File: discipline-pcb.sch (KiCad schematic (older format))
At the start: 22 parts, among them J1 AVR-ISP-6, U1 ATmega32A-PU, Y1 Crystal

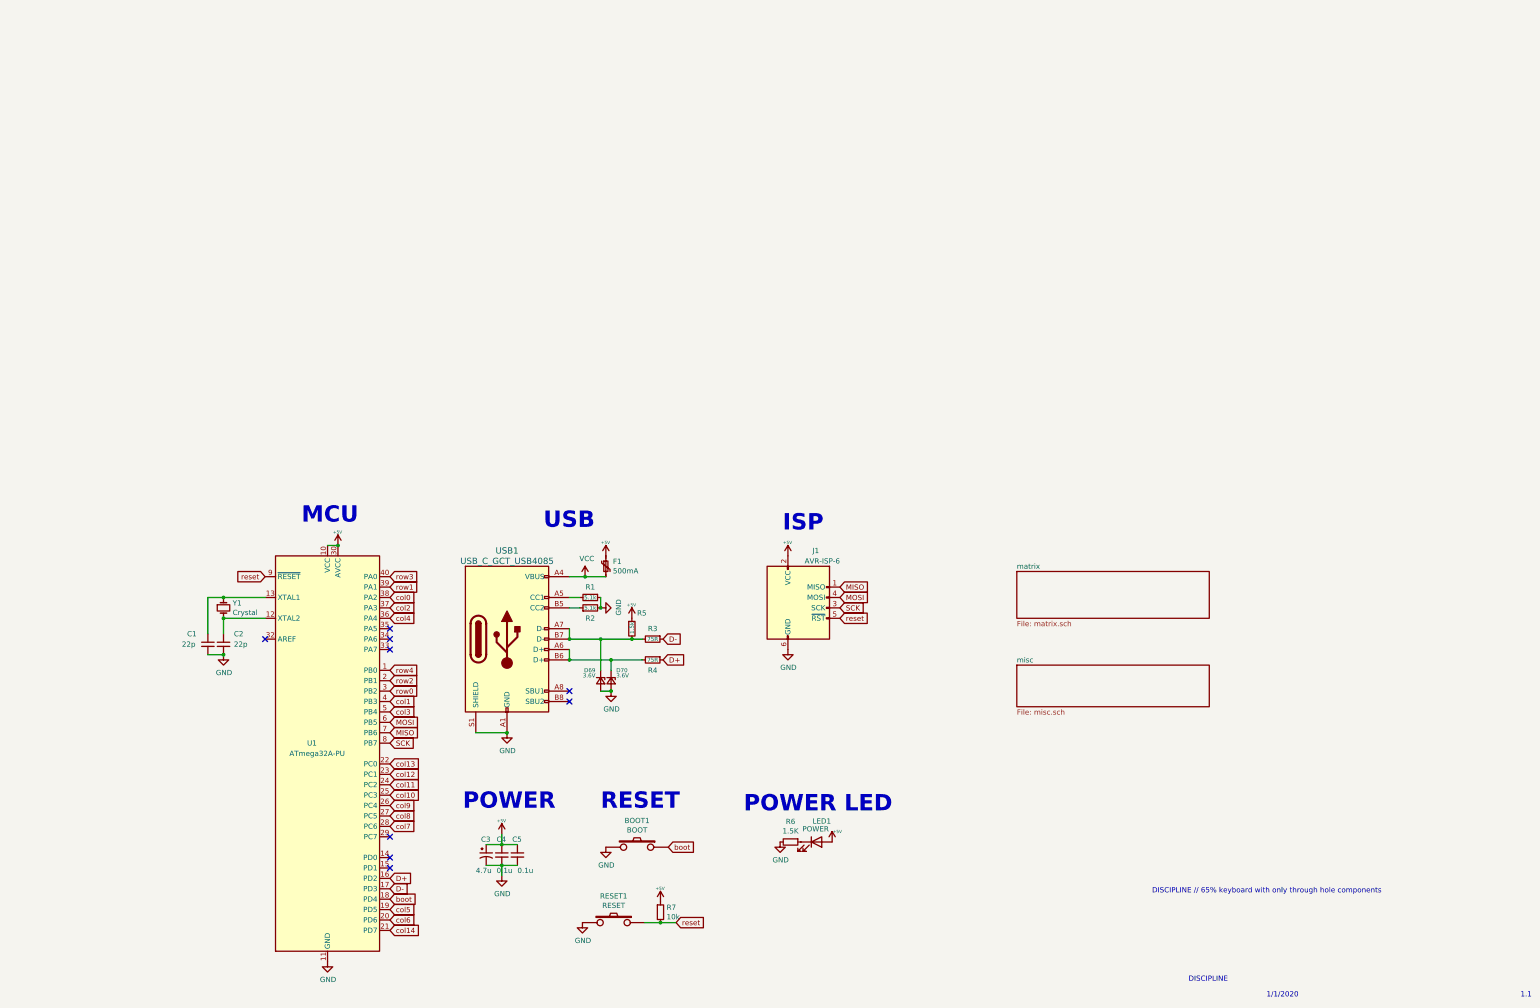
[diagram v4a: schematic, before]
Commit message: Add power, oled, ble modules
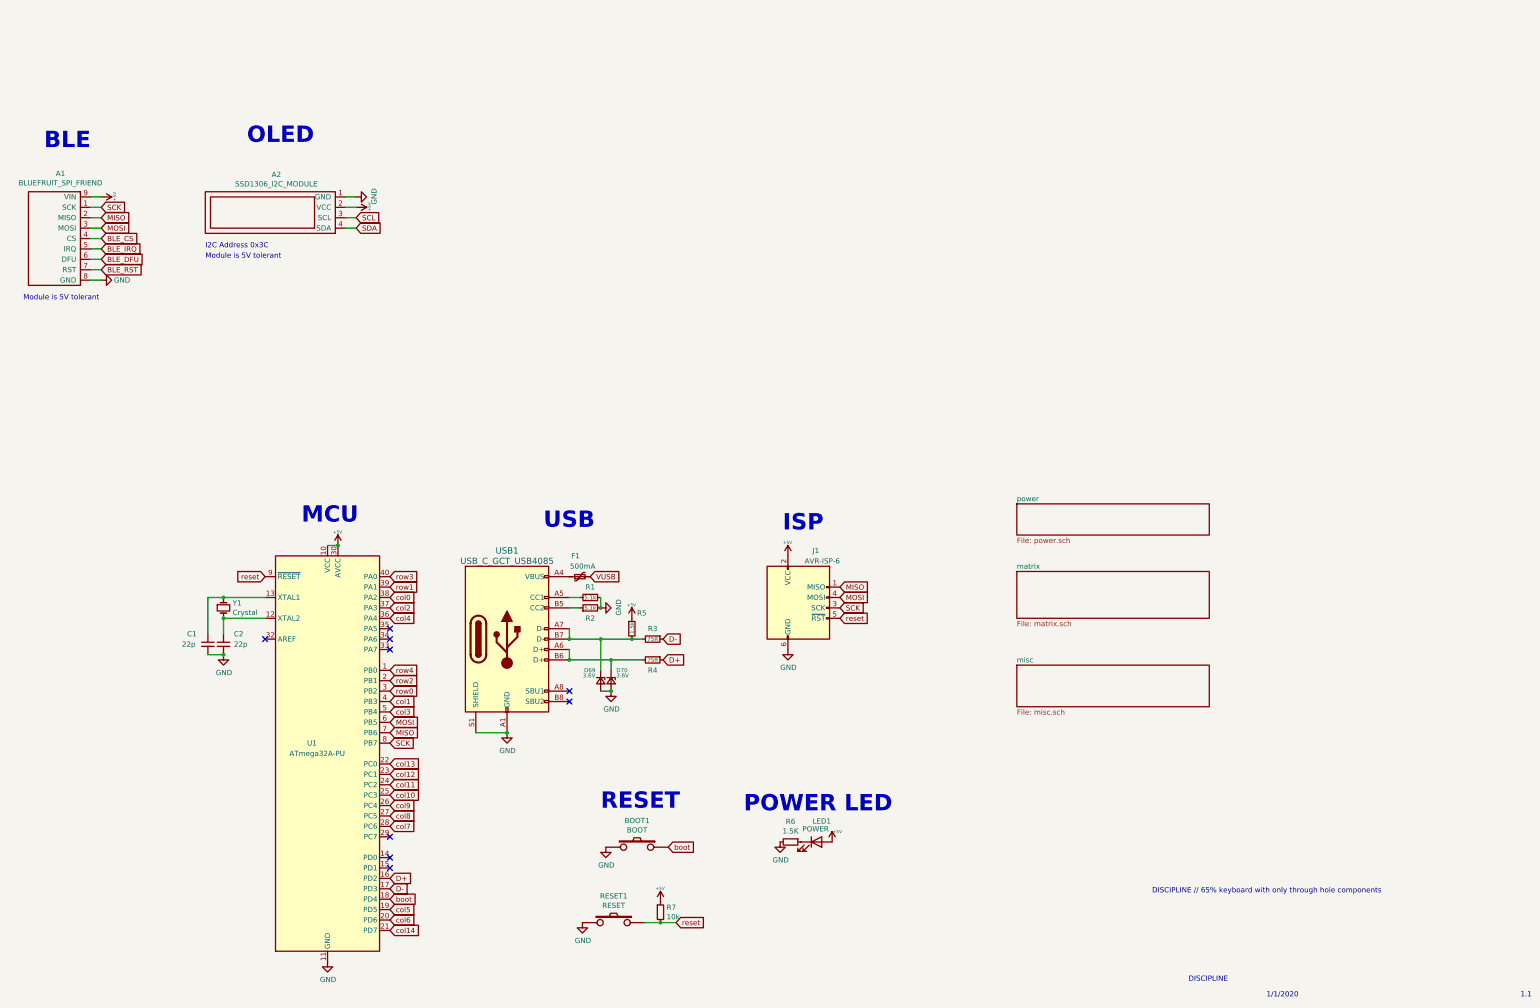
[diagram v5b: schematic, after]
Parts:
- removed C3: 4.7u, cftkb:CP_Radial_D4.0mm_P1.50mm, symbol Device:CP1_Small
- removed C4, C5: 0.1u, cftkb:C_Disc_D4.3mm_W1.9mm_P5.00mm, symbol Device:C_Small
- added A1: BLUEFRUIT_SPI_FRIEND, Gigahawk:BLUEFRUIT_SPI_FRIEND, symbol gigahawk:BLUEFRUIT_SPI_FRIEND
- added A2: SSD1306_I2C_MODULE, Gigahawk:SSD1306_MODULE_128x32, symbol gigahawk:SSD1306_I2C_MODULE
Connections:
- net +5V: now also A1.9 (VIN), A2.2 (VCC); no longer F1.1
- net GND: now also A1.8 (GND), A2.1 (GND)
- net MISO: now also A1.2 (MISO)
- net MOSI: now also A1.3 (MOSI)
- net SCK: now also A1.1 (SCK)
- net VCC: no longer names the net of USB1.A4 (VBUS), USB1.A9 (VBUS), USB1.B4 (VBUS), USB1.B9 (VBUS)
- net VCC: now also F1.1; no longer F1.2
- new net BLE_CS: A1.4 (CS)
- new net BLE_DFU: A1.6 (DFU)
- new net BLE_IRQ: A1.5 (IRQ)
- new net BLE_RST: A1.7 (RST)
- new net SCL: A2.3 (SCL)
- new net SDA: A2.4 (SDA)
- new net VUSB: F1.2
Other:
- note added: "BLE"
- note added: "I2C Address 0x3C"
- note added: "Module is 5V tolerant"
- note added: "Module is 5V tolerant\n"
- note added: "OLED"
- note removed: "POWER"
- moved on the sheet: F1
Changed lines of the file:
@@
 $Descr A3 16535 11693
 encoding utf-8
-Sheet 1 3
+Sheet 1 4
 Title ""
 Date ""
@@
 $EndComp
 $Comp
-L power:VCC #PWR0105
-U 1 1 5D2F7246
-P 6450 7000
-F 0 "#PWR0105" H 6450 6850 50  0001 C CNN
-F 1 "VCC" H 6467 7173 50  0000 C CNN
-F 2 "" H 6450 7000 50  0001 C CNN
-F 3 "" H 6450 7000 50  0001 C CNN
-	1    6450 7000
-	1    0    0    -1
-$EndComp
-$Comp
 L Device:Polyfuse_Small F1
 U 1 1 5D2F73B7
-P 6650 6900
-F 0 "F1" H 6718 6946 50  0000 L CNN
-F 1 "500mA" H 6718 6855 50  0000 L CNN
-F 2 "cftkb:polyfuse_5.1mm" H 6700 6700 50  0001 L CNN
-F 3 "~" H 6650 6900 50  0001 C CNN
-	1    6650 6900
-	1    0    0    -1
+P 6400 7000
+F 0 "F1" V 6600 7000 50  0000 L CNN
+F 1 "500mA" V 6500 6850 50  0000 L CNN
+F 2 "cftkb:polyfuse_5.1mm" H 6450 6800 50  0001 L CNN
+F 3 "~" H 6400 7000 50  0001 C CNN
+	1    6400 7000
+	0    -1   -1   0
 $EndComp
 $Comp
 L power:+5V #PWR0110
 U 1 1 5D31262D
-P 6650 6800
-F 0 "#PWR0110" H 6650 6890 20  0001 C CNN
-F 1 "+5V" H 6646 6928 30  0000 C CNN
-F 2 "" H 6650 6800 60  0000 C CNN
-F 3 "" H 6650 6800 60  0000 C CNN
-	1    6650 6800
-	1    0    0    -1
-$EndComp
-$Comp
-L Device:CP1_Small C3
-U 1 1 5D175B8C
-P 5500 9675
-F 0 "C3" H 5450 9825 50  0000 L CNN
-F 1 "4.7u" H 5400 9525 50  0000 L CNN
-F 2 "cftkb:CP_Radial_D4.0mm_P1.50mm" H 5500 9675 50  0001 C CNN
-F 3 "~" H 5500 9675 50  0001 C CNN
-	1    5500 9675
-	1    0    0    -1
-$EndComp
-$Comp
-L Device:C_Small C4
-U 1 1 5D176D89
-P 5650 9675
-F 0 "C4" H 5600 9825 50  0000 L CNN
-F 1 "0.1u" H 5600 9525 50  0000 L CNN
-F 2 "cftkb:C_Disc_D4.3mm_W1.9mm_P5.00mm" H 5650 9675 50  0001 C CNN
-F 3 "~" H 5650 9675 50  0001 C CNN
-	1    5650 9675
-	1    0    0    -1
-$EndComp
-$Comp
-L Device:C_Small C5
-U 1 1 5D176ED3
-P 5800 9675
-F 0 "C5" H 5750 9825 50  0000 L CNN
-F 1 "0.1u" H 5800 9525 50  0000 L CNN
-F 2 "cftkb:C_Disc_D4.3mm_W1.9mm_P5.00mm" H 5800 9675 50  0001 C CNN
-F 3 "~" H 5800 9675 50  0001 C CNN
-	1    5800 9675
-	1    0    0    -1
-$EndComp
-Wire Wire Line
-	5500 9575 5650 9575
-Connection ~ 5650 9575
-Wire Wire Line
-	5650 9575 5800 9575
-$Comp
-L power:+5V #PWR0111
-U 1 1 5D193DAD
-P 5650 9475
-F 0 "#PWR0111" H 5650 9565 20  0001 C CNN
-F 1 "+5V" H 5646 9603 30  0000 C CNN
-F 2 "" H 5650 9475 60  0000 C CNN
-F 3 "" H 5650 9475 60  0000 C CNN
-	1    5650 9475
-	1    0    0    -1
-$EndComp
-Wire Wire Line
-	5650 9575 5650 9475
-Wire Wire Line
-	5500 9775 5650 9775
-Connection ~ 5650 9775
-Wire Wire Line
-	5650 9775 5800 9775
-Wire Wire Line
-	5650 9775 5650 9875
+P 1800 3350
+F 0 "#PWR0110" H 1800 3440 20  0001 C CNN
+F 1 "+5V" H 1796 3478 30  0000 C CNN
+F 2 "" H 1800 3350 60  0000 C CNN
+F 3 "" H 1800 3350 60  0000 C CNN
+	1    1800 3350
+	0    1    1    0
+$EndComp
 $Comp
 L power:+5V #PWR0108
@@
 NoConn ~ 4575 9800
 $Comp
-L power:GND #PWR0112
-U 1 1 5DA49277
-P 5650 9875
-F 0 "#PWR0112" H 5650 9625 50  0001 C CNN
-F 1 "GND" H 5655 9702 50  0000 C CNN
-F 2 "" H 5650 9875 50  0001 C CNN
-F 3 "" H 5650 9875 50  0001 C CNN
-	1    5650 9875
-	1    0    0    -1
-$EndComp
-$Comp
 L MCU_Microchip_ATmega:ATmega32A-PU U1
 U 1 1 5DF0B623
@@
 Text Notes 8350 6575 0    157  ~ 31
 ISP
-Text Notes 5275 9250 0    157  ~ 31
-POWER
 Text Notes 6600 9250 0    157  ~ 31
 RESET
@@
 	1    0    0    -1
 $EndComp
-Wire Wire Line
-	6300 7000 6450 7000
-Wire Wire Line
-	6450 7000 6650 7000
-Connection ~ 6450 7000
 Wire Wire Line
 	5400 8500 5700 8500
@@
 F1 "misc.sch" 50
 $EndSheet
+$Comp
+L gigahawk:SSD1306_I2C_MODULE A2
+U 1 1 5F28E9FA
+P 4050 3300
+F 0 "A2" H 4617 3135 50  0000 C CNN
+F 1 "SSD1306_I2C_MODULE" H 4617 3226 50  0000 C CNN
+F 2 "Gigahawk:SSD1306_MODULE_128x32" H 4650 3750 50  0001 C CNN
+F 3 "" H 4100 3450 50  0001 C CNN
+	1    4050 3300
+	-1   0    0    1
+$EndComp
+$Comp
+L gigahawk:BLUEFRUIT_SPI_FRIEND A1
+U 1 1 5F29009B
+P 1350 3750
+F 0 "A1" H 1408 4375 50  0000 C CNN
+F 1 "BLUEFRUIT_SPI_FRIEND" H 1408 4284 50  0000 C CNN
+F 2 "Gigahawk:BLUEFRUIT_SPI_FRIEND" H 700 4150 50  0001 C CNN
+F 3 "" H 700 4150 50  0001 C CNN
+	1    1350 3750
+	1    0    0    -1
+$EndComp
+Text GLabel 6500 7000 2    50   Input ~ 0
+VUSB
+$Sheet
+S 10600 6300 1850 300
+U 5F36D657
+F0 "power" 50
+F1 "power.sch" 50
+$EndSheet
+Text Notes 1250 2900 0    157  ~ 31
+BLE
+Wire Wire Line
+	1700 3350 1800 3350
+Text GLabel 1800 3650 2    50   Input ~ 0
+MOSI
+Text GLabel 1800 3550 2    50   Input ~ 0
+MISO
+Text GLabel 1800 3450 2    50   Input ~ 0
+SCK
+Text GLabel 1800 3750 2    50   Input ~ 0
+BLE_CS
+Text GLabel 1800 3850 2    50   Input ~ 0
+BLE_IRQ
+Text GLabel 1800 3950 2    50   Input ~ 0
+BLE_DFU
+Text GLabel 1800 4050 2    50   Input ~ 0
+BLE_RST
+$Comp
+L power:GND #PWR?
+U 1 1 5F37DA59
+P 1800 4150
+F 0 "#PWR?" H 1800 3900 50  0001 C CNN
+F 1 "GND" V 1800 3950 50  0000 C CNN
+F 2 "" H 1800 4150 50  0001 C CNN
+F 3 "" H 1800 4150 50  0001 C CNN
+	1    1800 4150
+	0    -1   -1   0
+$EndComp
+Wire Wire Line
+	1700 4150 1800 4150
+Wire Wire Line
+	1700 4050 1800 4050
+Wire Wire Line
+	1700 3950 1800 3950
+Wire Wire Line
+	1700 3850 1800 3850
+Wire Wire Line
+	1700 3750 1800 3750
+Wire Wire Line
+	1700 3650 1800 3650
+Wire Wire Line
+	1700 3550 1800 3550
+Wire Wire Line
+	1700 3450 1800 3450
+Text Notes 3200 2850 0    157  ~ 31
+OLED
+$Comp
+L power:GND #PWR?
+U 1 1 5F38423A
+P 4250 3350
+F 0 "#PWR?" H 4250 3100 50  0001 C CNN
+F 1 "GND" H 4255 3177 50  0000 C CNN
+F 2 "" H 4250 3350 50  0001 C CNN
+F 3 "" H 4250 3350 50  0001 C CNN
+	1    4250 3350
+	0    -1   -1   0
+$EndComp
+Text Notes 1050 4350 0    50   ~ 0
+Module is 5V tolerant\n
+Text Notes 2800 3950 0    50   ~ 0
+Module is 5V tolerant
+Wire Wire Line
+	4150 3350 4250 3350
+$Comp
+L power:+5V #PWR?
+U 1 1 5F385D89
+P 4250 3450
+F 0 "#PWR?" H 4250 3540 20  0001 C CNN
+F 1 "+5V" H 4246 3578 30  0000 C CNN
+F 2 "" H 4250 3450 60  0000 C CNN
+F 3 "" H 4250 3450 60  0000 C CNN
+	1    4250 3450
+	0    1    1    0
+$EndComp
+Wire Wire Line
+	4150 3450 4250 3450
+Text GLabel 4250 3550 2    50   Input ~ 0
+SCL
+Text GLabel 4250 3650 2    50   Input ~ 0
+SDA
+Wire Wire Line
+	4150 3550 4250 3550
+Wire Wire Line
+	4150 3650 4250 3650
+Text Notes 2800 3850 0    50   ~ 0
+I2C Address 0x3C
 $EndSCHEMATC

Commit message: Add rotary encoder
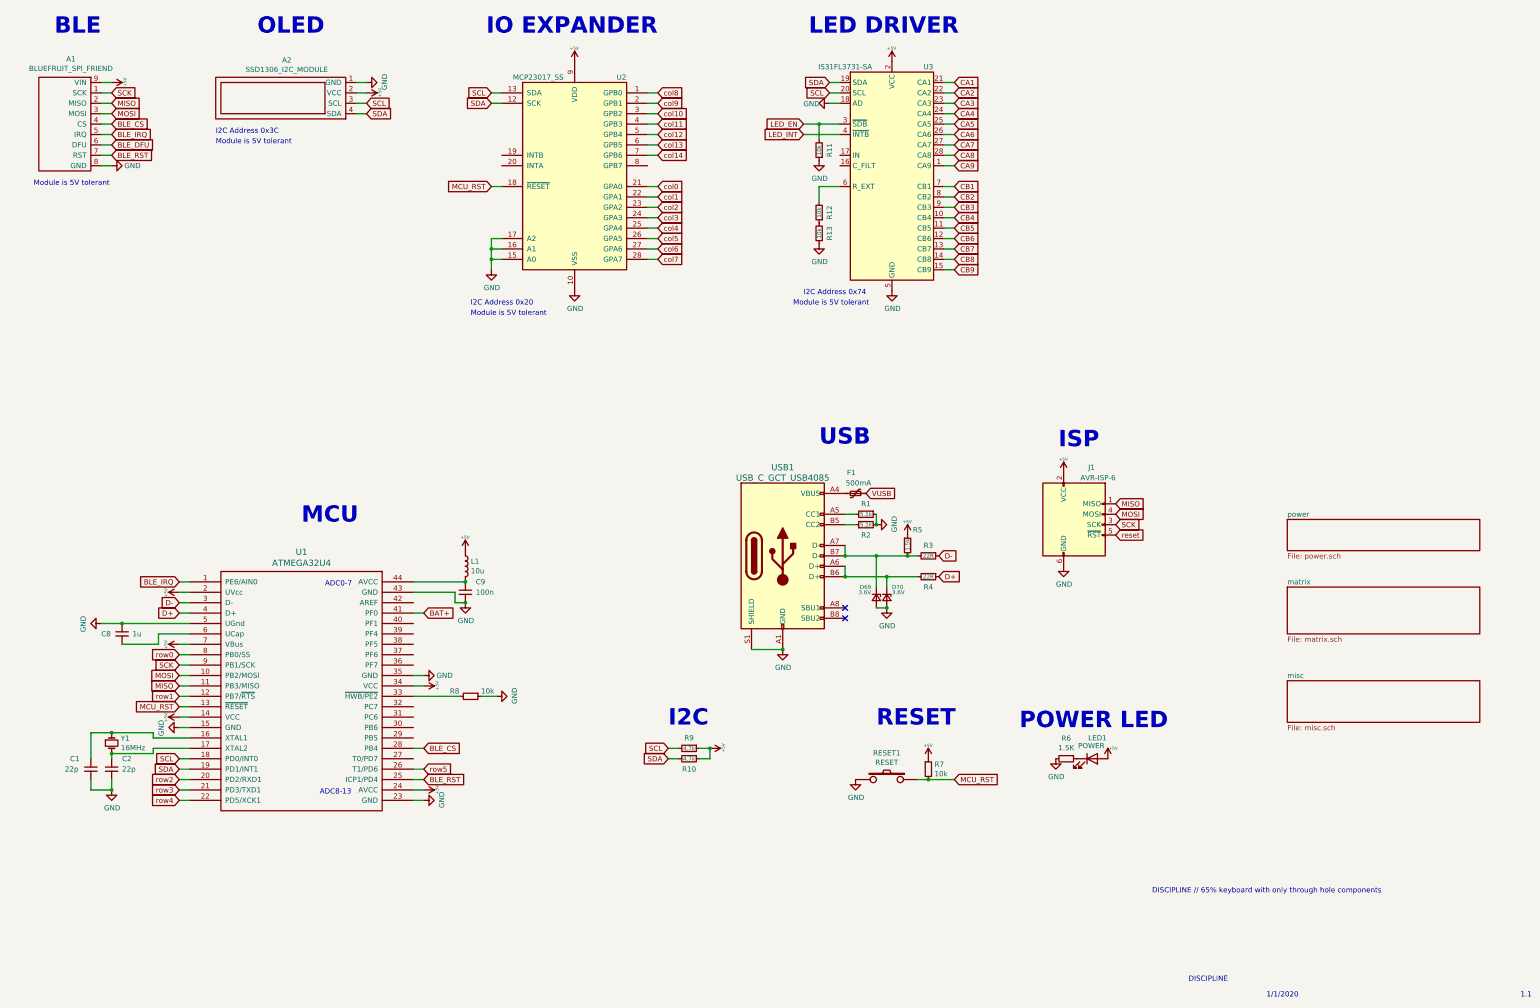
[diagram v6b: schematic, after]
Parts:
- removed BOOT1: BOOT, cftkb:SW_PUSH_6mm, symbol keyboard_parts:SW_PUSH
- removed U1: ATmega32A-PU, cftkb:DIP-40_W15.24mm, symbol MCU_Microchip_ATmega:ATmega32A-PU
- added C8: 1u, cftkb:C_Disc_D3.0mm_W1.6mm_P2.50mm, symbol Device:C_Small
- added C9: 100n, cftkb:C_Disc_D3.0mm_W1.6mm_P2.50mm, symbol Device:C_Small
- added L1: 10u, symbol Device:L
- added R10, R9: 4.7k, cftkb:R_Axial_DIN0204_L3.6mm_D1.6mm_P5.08mm_Horizontal, symbol Device:R_Small
- added R11, R12, R13, R8: 10k, cftkb:R_Axial_DIN0204_L3.6mm_D1.6mm_P5.08mm_Horizontal, symbol Device:R_Small
- added U1: ATMEGA32U4, Package_QFP:TQFP-44_10x10mm_P0.8mm, symbol keyboard_parts:ATMEGA32U4
- added U2: MCP23017_SS, Package_SO:SSOP-28_5.3x10.2mm_P0.65mm, symbol Interface_Expansion:MCP23017_SS
- added U3: IS31FL3731-SA, Package_SO:SSOP-28_5.3x10.2mm_P0.65mm, symbol Driver_LED:IS31FL3731-SA
- R3, R4: value 75R -> 22R
- Y1: value Crystal -> 16MHz
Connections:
- net +5V: now also L1.1, R10.1, R9.1, U1.14 (VCC), U1.2 (UVcc), U1.24 (AVCC), U1.34 (VCC), U1.7 (VBus), U2.9 (VDD), U3.2 (VCC)
- net BLE_CS: now also U1.28 (PB4)
- net BLE_IRQ: now also U1.1 (PE6/AIN0)
- net BLE_RST: now also U1.25 (ICP1/PD4)
- net D+: now also U1.4 (D+)
- net D-: now also U1.3 (D-)
- net GND: now also C8.1, C9.2, R11.1, R13.1, R8.1, U1.15 (GND), U1.23 (GND), U1.35 (GND), U1.43 (GND), U1.5 (UGnd), U2.10 (VSS), U2.15 (A0), U2.16 (A1), U2.17 (A2), U3.18 (AD), U3.5 (GND)
- net MISO: now also U1.11 (PB3/MISO)
- net MOSI: now also U1.10 (PB2/MOSI)
- net SCK: now also U1.9 (PB1/SCK)
- net SCL: now also R9.2, U1.18 (PD0/INT0), U2.13 (SDA), U3.20 (SCL)
- net SDA: now also R10.2, U1.19 (PD1/INT1), U2.12 (SCK), U3.19 (SDA)
- net col0: now also U2.21 (GPA0)
- net col1: now also U2.22 (GPA1)
- net col10: now also U2.3 (GPB2)
- net col11: now also U2.4 (GPB3)
- net col12: now also U2.5 (GPB4)
- net col13: now also U2.6 (GPB5)
- net col14: now also U2.7 (GPB6)
- net col2: now also U2.23 (GPA2)
- net col3: now also U2.24 (GPA3)
- net col4: now also U2.25 (GPA4)
- net col5: now also U2.26 (GPA5)
- net col6: now also U2.27 (GPA6)
- net col7: now also U2.28 (GPA7)
- net col8: now also U2.1 (GPB0)
- net col9: now also U2.2 (GPB1)
- net reset: no longer R7.2, RESET1.1
- net row0: now also U1.8 (PB0/SS)
- net row1: now also U1.12 (PB7/~RTS)
- net row2: now also U1.20 (PD2/RXD1)
- net row3: now also U1.21 (PD3/TXD1)
- net row4: now also U1.22 (PD5/XCK1)
- net at C2.1, Y1.2: now also U1.17 (XTAL2)
- net at C1.1, Y1.1: now also U1.16 (XTAL1)
- new net: R8.2, U1.33 (~HWB/PE2)
- new net: C9.1, L1.2, U1.44 (AVCC)
- new net: C8.2, U1.6 (UCap)
- new net: R12.2, U3.6 (R_EXT)
- new net: R12.1, R13.2
- new net BAT+: U1.41 (PF0)
- new net CA1: U3.21 (CA1)
- new net CA2: U3.22 (CA2)
- new net CA3: U3.23 (CA3)
- new net CA4: U3.24 (CA4)
- new net CA5: U3.25 (CA5)
- new net CA6: U3.26 (CA6)
- new net CA7: U3.27 (CA7)
- new net CA8: U3.28 (CA8)
- new net CA9: U3.1 (CA9)
- new net CB1: U3.7 (CB1)
- new net CB2: U3.8 (CB2)
- new net CB3: U3.9 (CB3)
- new net CB4: U3.10 (CB4)
- new net CB5: U3.11 (CB5)
- new net CB6: U3.12 (CB6)
- new net CB7: U3.13 (CB7)
- new net CB8: U3.14 (CB8)
- new net CB9: U3.15 (CB9)
- new net LED_EN: R11.2, U3.3 (~SDB)
- new net LED_INT: U3.4 (~INTB)
- new net MCU_RST: R7.2, RESET1.1, U1.13 (~RESET), U2.18 (~RESET~)
- new net row5: U1.26 (T1/PD6)
- no-connect marks 9 -> 2
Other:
- note added: "ADC0-7\n"
- note added: "ADC8-13\n"
- note added: "I2C"
- note added: "I2C Address 0x20"
- note added: "I2C Address 0x74"
- note added: "IO EXPANDER"
- note added: "LED DRIVER"
- moved on the sheet: A1, A2, C1, C2, D69, D70, F1, J1, LED1, R1, R2, R3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
